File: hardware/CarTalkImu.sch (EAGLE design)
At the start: 11 parts, among them J4 1X10, J5 1X10, U3 MPU9250, U4 NEO-M8

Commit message: Finalized Rev 1A schematic and layout.
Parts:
- added C1, C3, C4, C5, C6, C7: 100n, CarTalkImu:C-USC0603
- added C10, C8: 10u, CarTalkImu:C-USC0603
- added C11, C9: 1u, CarTalkImu:C-USC0603
- added C2: 10n, CarTalkImu:C-USC0603
- added R1, R2, R3, R4, R5: 10k, CarTalkImu:R-US_R0603
- added R10, R11, R6, R7, R8, R9: 220, CarTalkImu:R-US_R0603
- added U1: LPS22HB, CarTalkImu:LPS22HB
- added X1: (no value), CarTalkImu:ESP-12
- U4: value NEO-M8 -> CAM-M8; device CarTalkImu:NEO-M8 -> CarTalkImu:CAM-M8
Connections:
- removed net XB_MULT2: J5.5
- removed net XB_MULT3: J5.9
- removed net XB_MULT5: J4.8
- removed net XB_MULT6: J5.10
- new net N$10: R6.2, U4.RXD/MOSI
- new net N$11: R7.2, U4.TXD/MISO
- new net N$12: R8.2, U4.SCL/SCLK
- new net N$13: R9.2, U4.SDA/CS
- new net N$14: U4.RF_IN, U4.RF_OUT
- new net N$15: R10.2, X1.TXD
- new net N$16: R11.2, X1.RXD
- new net N$4: C1.1, U3.REGOUT
- new net N$6: R1.1, X1.GPIO0
- new net N$7: R2.1, X1.GPIO2
- new net N$8: R3.1, X1.GPIO15
- new net N$9: R4.1, X1.CH_PD
- new net XB_MULT2/PRESS_CS: J5.5, U1.CS
- new net XB_MULT3/TMPLSE: J5.9, U4.TMPLSE
- new net XB_MULT5/MPU_CS: J4.8, U3./CS
- new net XB_MULT6/GPS_CS: J5.10, R9.1
- net +3V3: now also C10.1, C11.1, C2.1, C3.1, C4.1, C5.1, C7.1, C8.1, C9.1, R1.2, R2.2, R4.2, R5.2, U1.VDD, U1.VDD_IO, U3.RESV_1, U3.VDD, U3.VDDIO, U4.VCC, U4.VCC_IO, U4.V_BCKP, X1.VCC
- net DGND: now also C1.2, C10.2, C11.2, C2.2, C3.2, C4.2, C5.2, C6.2, C7.2, C8.2, C9.2, R3.2, U1.GND, U3.FSYNC, U3.GND, U3.RESV_20, U4.D_SEL, U4.GND, X1.GND
- net SPI0_CLK: now also R8.1, U1.SCL/SPC, U3.SCL/SCLK
- net SPI0_MISO: now also R7.1, U1.SDO/SA0, U3.AD0/SDO
- net SPI0_MOSI: now also R6.1, U1.SDA/SDI/SDO, U3.SDA/SDI
- net XB_NRST: now also C6.1, R5.1, U4./RST, X1.RESET
- net XB_UART_RX: now also R10.1
- net XB_UART_TX: now also R11.1
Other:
- moved on the sheet: U3

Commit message: Re-finalized design and layout.
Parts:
- X1: value (none) -> ESP-12
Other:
- moved on the sheet: C10, C11, C5, C6, C7, C8, C9, R1, R10, R11, R2, R3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

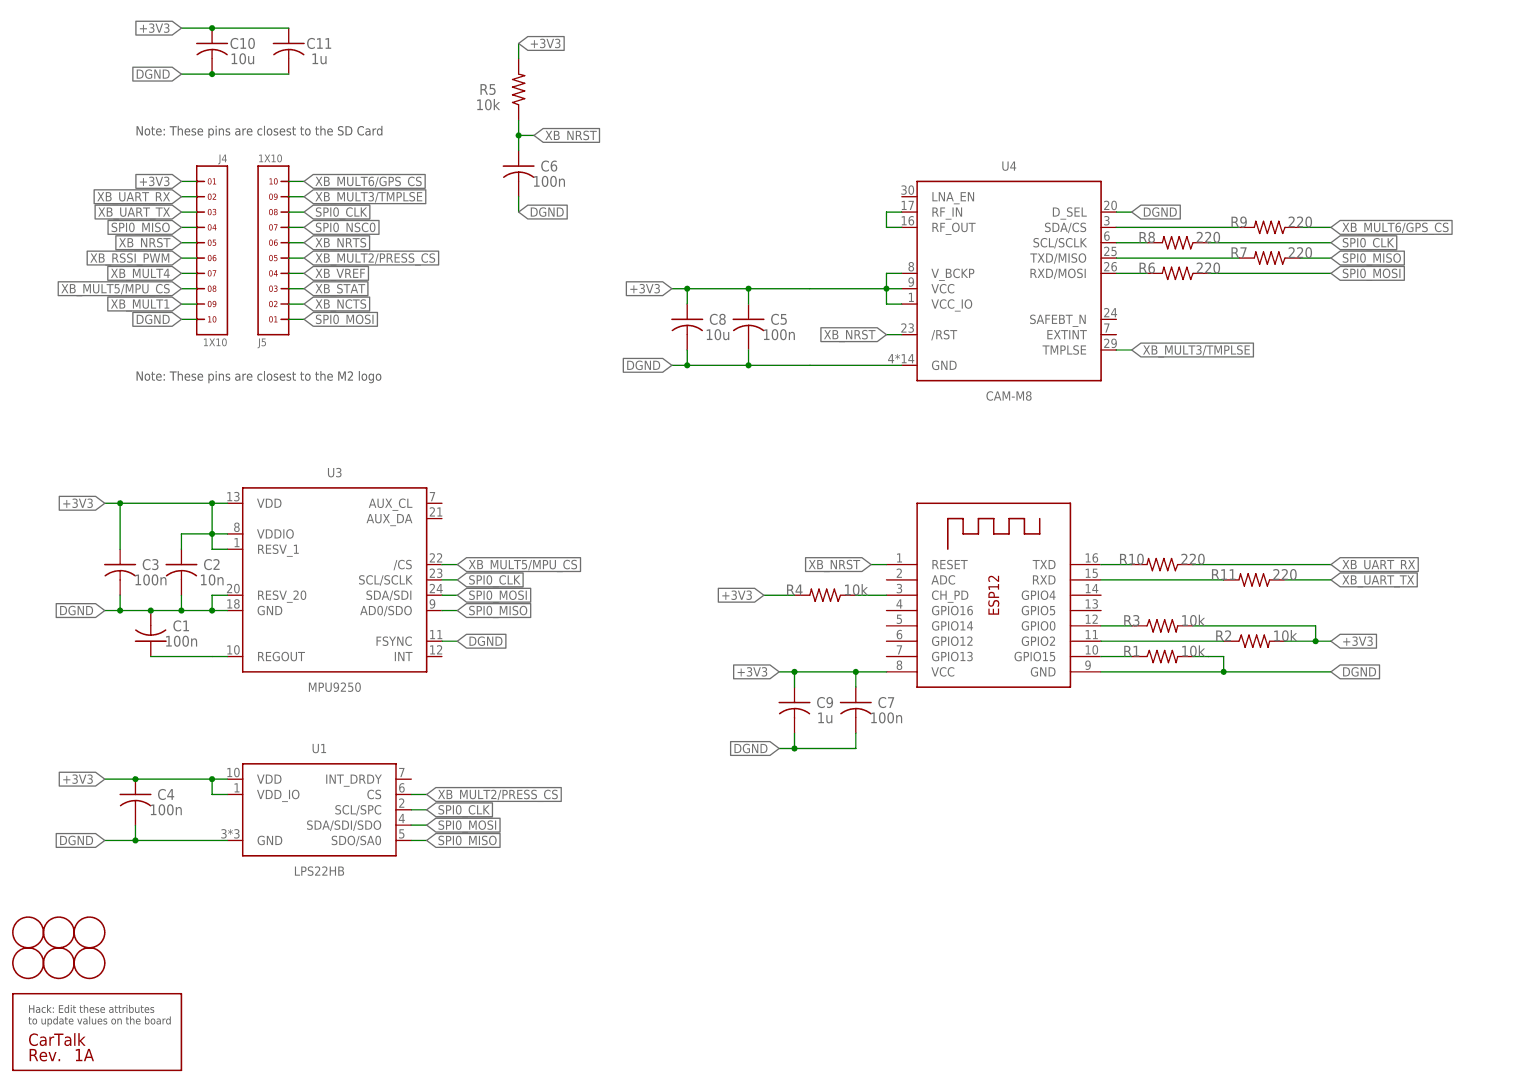
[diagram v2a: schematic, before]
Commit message: Replaced LPS22 part with BME680 part. Upated board layout.
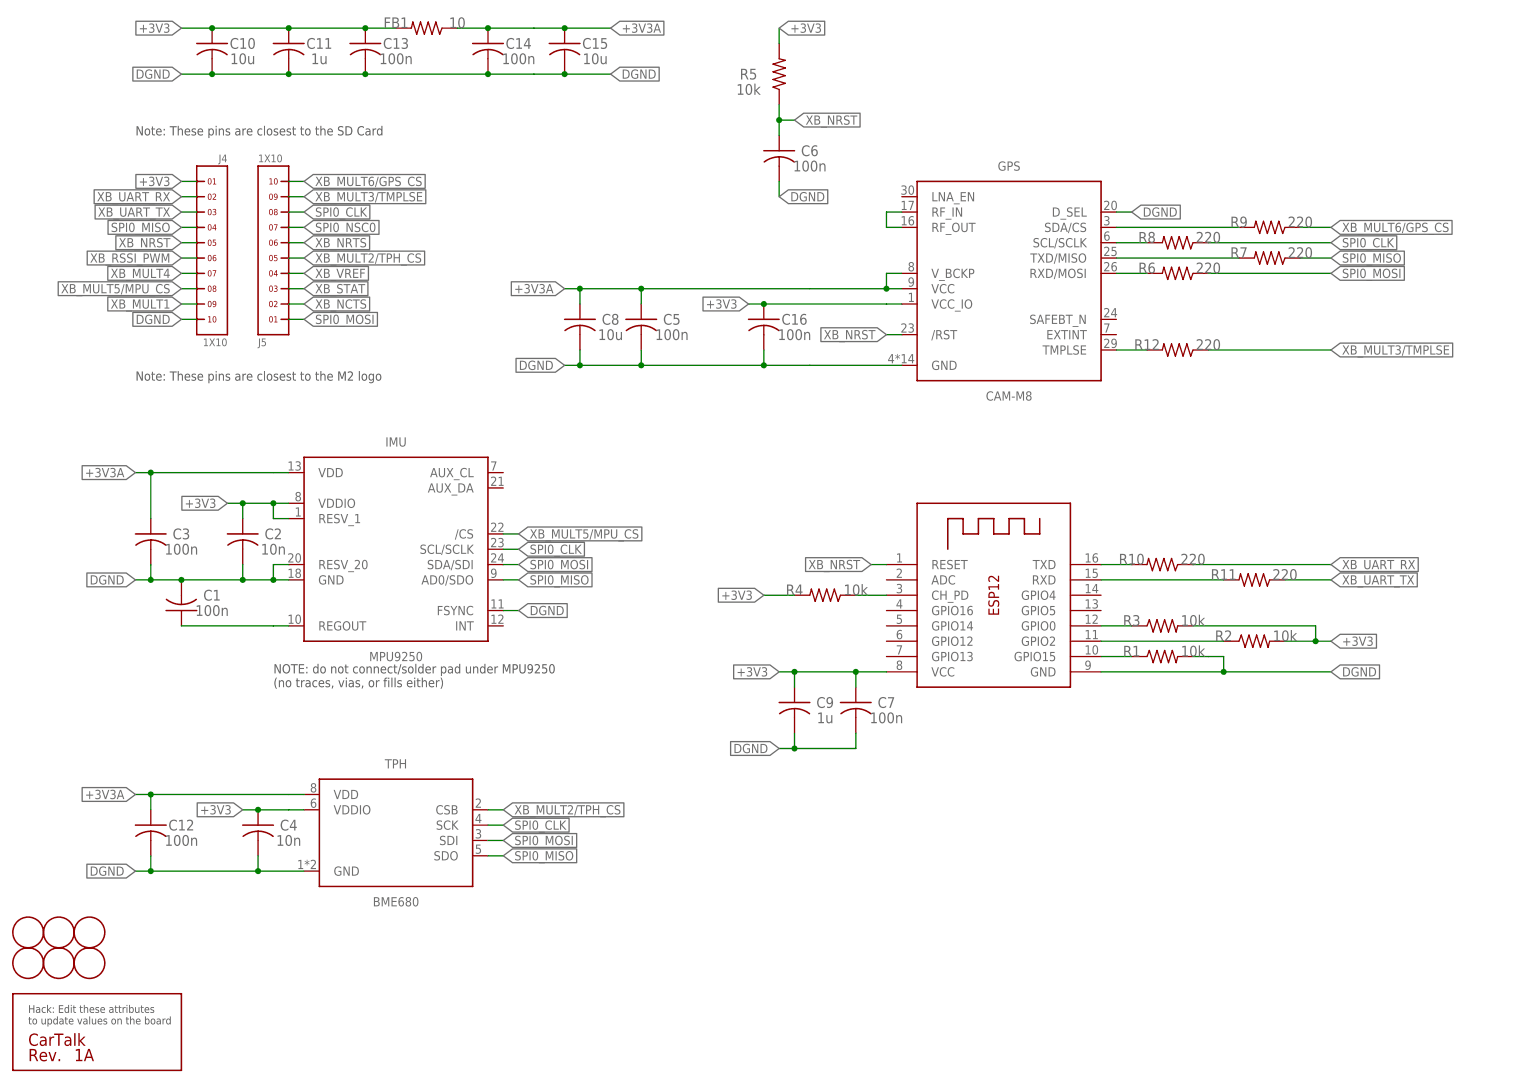
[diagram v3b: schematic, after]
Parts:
- removed U1: LPS22HB, CarTalkImu:LPS22HB
- removed U3: MPU9250, CarTalkImu:MPU9250
- added C12, C13, C14, C16: 100n, CarTalkImu:C-USC0603
- added C15: 10u, CarTalkImu:C-USC0805
- added FB1: 10, CarTalkImu:R-US_R0603
- added IMU: MPU9250, CarTalkImu:MPU9250
- added R12: 220, CarTalkImu:R-US_R0603
- added TPH: BME680, CarTalkImu:BME680
- C10, C8: device CarTalkImu:C-USC0603 -> CarTalkImu:C-USC0805
- C4: value 100n -> 10n
- renumbered U4 to GPS, X1 to WIFI
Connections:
- removed net XB_MULT2/PRESS_CS: J5.5, U1.CS
- new net +3V3A: C12.1, C14.1, C15.1, C3.1, C5.1, C8.1, FB1.1, GPS.VCC, GPS.V_BCKP, IMU.VDD, TPH.VDD
- new net N$18: GPS.TMPLSE, R12.2
- new net XB_MULT2/TPH_CS: J5.5, TPH.CSB
- net +3V3: now also C13.1, C16.1, FB1.2, IMU.RESV_1, IMU.VDDIO, TPH.VDDIO; no longer C3.1, C5.1, C8.1, GPS.VCC, GPS.V_BCKP, U1.VDD, U1.VDD_IO, U3.RESV_1, U3.VDD, U3.VDDIO
- net DGND: now also C12.2, C13.2, C14.2, C15.2, C16.2, IMU.FSYNC, IMU.GND, IMU.RESV_20, TPH.GND; no longer U1.GND, U3.FSYNC, U3.GND, U3.RESV_20
- net N$4: now also IMU.REGOUT; no longer U3.REGOUT
- net SPI0_CLK: now also IMU.SCL/SCLK, TPH.SCK; no longer U1.SCL/SPC, U3.SCL/SCLK
- net SPI0_MISO: now also IMU.AD0/SDO, TPH.SDO; no longer U1.SDO/SA0, U3.AD0/SDO
- net SPI0_MOSI: now also IMU.SDA/SDI, TPH.SDI; no longer U1.SDA/SDI/SDO, U3.SDA/SDI
- net XB_MULT3/TMPLSE: now also R12.1; no longer GPS.TMPLSE
- net XB_MULT5/MPU_CS: now also IMU./CS; no longer U3./CS
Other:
- note added: "NOTE: do not connect/solder pad under MPU9250 (no traces, vias, or fills either)"
- moved on the sheet: C1, C2, C3, C4, C5, C6, C8, R5

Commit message: Fixed minor layout/DFM issues
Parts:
- renumbered IMU to MPU
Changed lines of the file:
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@@
 <grid distance="0.1" unitdist="inch" unit="inch" style="lines" multiple="1" display="no" altdistance="0.01" altunitdist="inch" altunit="inch"/>
 <layers>
-<layer number="1" name="Top" color="4" fill="1" visible="yes" active="no"/>
-<layer number="2" name="Route2" color="1" fill="3" visible="yes" active="no"/>
-<layer number="15" name="Route15" color="4" fill="6" visible="yes" active="no"/>
-<layer number="16" name="Bottom" color="1" fill="1" visible="yes" active="no"/>
-<layer number="17" name="Pads" color="2" fill="1" visible="yes" active="no"/>
-<layer number="18" name="Vias" color="2" fill="1" visible="yes" active="no"/>
-<layer number="19" name="Unrouted" color="6" fill="1" visible="yes" active="no"/>
-<layer number="20" name="Dimension" color="15" fill="1" visible="yes" active="no"/>
-<layer number="21" name="tPlace" color="7" fill="1" visible="yes" active="no"/>
-<layer number="22" name="bPlace" color="7" fill="1" visible="yes" active="no"/>
-<layer number="23" name="tOrigins" color="15" fill="1" visible="yes" active="no"/>
-<layer number="24" name="bOrigins" color="15" fill="1" visible="yes" active="no"/>
-<layer number="25" name="tNames" color="7" fill="1" visible="yes" active="no"/>
-<layer number="26" name="bNames" color="7" fill="1" visible="yes" active="no"/>
-<layer number="27" name="tValues" color="7" fill="1" visible="yes" active="no"/>
-<layer number="28" name="bValues" color="7" fill="1" visible="yes" active="no"/>
+<layer number="1" name="Top" color="4" fill="1" visible="no" active="no"/>
+<layer number="2" name="Route2" color="1" fill="3" visible="no" active="no"/>
+<layer number="15" name="Route15" color="4" fill="6" visible="no" active="no"/>
+<layer number="16" name="Bottom" color="1" fill="1" visible="no" active="no"/>
+<layer number="17" name="Pads" color="2" fill="1" visible="no" active="no"/>
+<layer number="18" name="Vias" color="2" fill="1" visible="no" active="no"/>
+<layer number="19" name="Unrouted" color="6" fill="1" visible="no" active="no"/>
+<layer number="20" name="Dimension" color="15" fill="1" visible="no" active="no"/>
+<layer number="21" name="tPlace" color="7" fill="1" visible="no" active="no"/>
+<layer number="22" name="bPlace" color="7" fill="1" visible="no" active="no"/>
+<layer number="23" name="tOrigins" color="15" fill="1" visible="no" active="no"/>
+<layer number="24" name="bOrigins" color="15" fill="1" visible="no" active="no"/>
+<layer number="25" name="tNames" color="7" fill="1" visible="no" active="no"/>
+<layer number="26" name="bNames" color="7" fill="1" visible="no" active="no"/>
+<layer number="27" name="tValues" color="7" fill="1" visible="no" active="no"/>
+<layer number="28" name="bValues" color="7" fill="1" visible="no" active="no"/>
 <layer number="29" name="tStop" color="7" fill="3" visible="no" active="no"/>
 <layer number="30" name="bStop" color="7" fill="6" visible="no" active="no"/>
@@
 <layer number="35" name="tGlue" color="7" fill="4" visible="no" active="no"/>
 <layer number="36" name="bGlue" color="7" fill="5" visible="no" active="no"/>
-<layer number="37" name="tTest" color="7" fill="1" visible="yes" active="no"/>
-<layer number="38" name="bTest" color="7" fill="1" visible="yes" active="no"/>
+<layer number="37" name="tTest" color="7" fill="1" visible="no" active="no"/>
+<layer number="38" name="bTest" color="7" fill="1" visible="no" active="no"/>
 <layer number="39" name="tKeepout" color="4" fill="11" visible="no" active="no"/>
 <layer number="40" name="bKeepout" color="1" fill="11" visible="no" active="no"/>
@@
 <layer number="44" name="Drills" color="7" fill="1" visible="no" active="no"/>
 <layer number="45" name="Holes" color="7" fill="1" visible="no" active="no"/>
-<layer number="46" name="Milling" color="3" fill="1" visible="yes" active="no"/>
-<layer number="47" name="Measures" color="7" fill="1" visible="yes" active="no"/>
-<layer number="48" name="Document" color="7" fill="1" visible="yes" active="no"/>
-<layer number="49" name="Reference" color="7" fill="1" visible="yes" active="no"/>
-<layer number="50" name="dxf" color="7" fill="1" visible="yes" active="no"/>
-<layer number="51" name="tDocu" color="7" fill="1" visible="yes" active="no"/>
-<layer number="52" name="bDocu" color="7" fill="1" visible="yes" active="no"/>
-<layer number="53" name="tGND_GNDA" color="7" fill="9" visible="yes" active="no"/>
-<layer number="54" name="bGND_GNDA" color="1" fill="9" visible="yes" active="no"/>
-<layer number="56" name="wert" color="7" fill="1" visible="yes" active="no"/>
-<layer number="57" name="tCAD" color="7" fill="1" visible="yes" active="no"/>
+<layer number="46" name="Milling" color="3" fill="1" visible="no" active="no"/>
+<layer number="47" name="Measures" color="7" fill="1" visible="no" active="no"/>
+<layer number="48" name="Document" color="7" fill="1" visible="no" active="no"/>
+<layer number="49" name="Reference" color="7" fill="1" visible="no" active="no"/>
+<layer number="50" name="dxf" color="7" fill="1" visible="no" active="no"/>
+<layer number="51" name="tDocu" color="7" fill="1" visible="no" active="no"/>
+<layer number="52" name="bDocu" color="7" fill="1" visible="no" active="no"/>
+<layer number="53" name="tGND_GNDA" color="7" fill="9" visible="no" active="no"/>
+<layer number="54" name="bGND_GNDA" color="1" fill="9" visible="no" active="no"/>
+<layer number="56" name="wert" color="7" fill="1" visible="no" active="no"/>
+<layer number="57" name="tCAD" color="7" fill="1" visible="no" active="no"/>
 <layer number="90" name="Modules" color="5" fill="1" visible="yes" active="yes"/>
 <layer number="91" name="Nets" color="2" fill="1" visible="yes" active="yes"/>
@@
 <part name="J4" library="CarTalkImu" deviceset="1X10" device=""/>
 <part name="J5" library="CarTalkImu" deviceset="1X10" device=""/>
-<part name="IMU" library="CarTalkImu" deviceset="MPU9250" device=""/>
+<part name="MPU" library="CarTalkImu" deviceset="MPU9250" device=""/>
 <part name="GPS" library="CarTalkImu" deviceset="CAM-M8" device=""/>
 <part name="FRAME1" library="CarTalkImu" deviceset="LETTER_L" device="">
@@
 <instance part="J4" gate="G$1" x="38.1" y="139.7" rot="MR0"/>
 <instance part="J5" gate="G$1" x="48.26" y="142.24" rot="MR180"/>
-<instance part="IMU" gate="G$1" x="68.58" y="91.44"/>
+<instance part="MPU" gate="G$1" x="68.58" y="91.44"/>
 <instance part="GPS" gate="G$1" x="170.18" y="137.16"/>
 <instance part="FRAME1" gate="G$1" x="0" y="0"/>
@@
 </segment>
 <segment>
-<pinref part="IMU" gate="G$1" pin="VDDIO"/>
+<pinref part="MPU" gate="G$1" pin="VDDIO"/>
 <wire x1="50.8" y1="99.06" x2="48.26" y2="99.06" width="0.1524" layer="91"/>
-<pinref part="IMU" gate="G$1" pin="RESV_1"/>
+<pinref part="MPU" gate="G$1" pin="RESV_1"/>
 <wire x1="50.8" y1="96.52" x2="48.26" y2="96.52" width="0.1524" layer="91"/>
 <wire x1="48.26" y1="96.52" x2="48.26" y2="99.06" width="0.1524" layer="91"/>
@@
 <wire x1="88.9" y1="86.36" x2="86.36" y2="86.36" width="0.1524" layer="91"/>
 <label x="88.9" y="86.36" size="1.524" layer="95" xref="yes"/>
-<pinref part="IMU" gate="G$1" pin="AD0/SDO"/>
+<pinref part="MPU" gate="G$1" pin="AD0/SDO"/>
 </segment>
 <segment>
@@
 </segment>
 <segment>
-<pinref part="IMU" gate="G$1" pin="/CS"/>
+<pinref part="MPU" gate="G$1" pin="/CS"/>
 <wire x1="86.36" y1="93.98" x2="88.9" y2="93.98" width="0.1524" layer="91"/>
 <label x="88.9" y="93.98" size="1.524" layer="95" xref="yes"/>
@@
 <wire x1="50.8" y1="86.36" x2="48.26" y2="86.36" width="0.1524" layer="91"/>
 <label x="25.4" y="86.36" size="1.524" layer="95" rot="R180" xref="yes"/>
-<pinref part="IMU" gate="G$1" pin="RESV_20"/>
+<pinref part="MPU" gate="G$1" pin="RESV_20"/>
 <wire x1="48.26" y1="86.36" x2="43.18" y2="86.36" width="0.1524" layer="91"/>
 <wire x1="43.18" y1="86.36" x2="33.02" y2="86.36" width="0.1524" layer="91"/>
@@
 <pinref part="C1" gate="G$1" pin="2"/>
 <junction x="33.02" y="86.36"/>
-<pinref part="IMU" gate="G$1" pin="GND"/>
+<pinref part="MPU" gate="G$1" pin="GND"/>
 </segment>
 <segment>
@@
 </segment>
 <segment>
-<pinref part="IMU" gate="G$1" pin="FSYNC"/>
+<pinref part="MPU" gate="G$1" pin="FSYNC"/>
 <wire x1="86.36" y1="81.28" x2="88.9" y2="81.28" width="0.1524" layer="91"/>
 <label x="88.9" y="81.28" size="1.524" layer="95" xref="yes"/>
@@
 <wire x1="86.36" y1="91.44" x2="88.9" y2="91.44" width="0.1524" layer="91"/>
 <label x="88.9" y="91.44" size="1.524" layer="95" xref="yes"/>
-<pinref part="IMU" gate="G$1" pin="SCL/SCLK"/>
+<pinref part="MPU" gate="G$1" pin="SCL/SCLK"/>
 </segment>
 <segment>
@@
 <wire x1="86.36" y1="88.9" x2="88.9" y2="88.9" width="0.1524" layer="91"/>
 <label x="88.9" y="88.9" size="1.524" layer="95" xref="yes"/>
-<pinref part="IMU" gate="G$1" pin="SDA/SDI"/>
+<pinref part="MPU" gate="G$1" pin="SDA/SDI"/>
 </segment>
 <segment>
@@
 <net name="N$4" class="0">
 <segment>
-<pinref part="IMU" gate="G$1" pin="REGOUT"/>
+<pinref part="MPU" gate="G$1" pin="REGOUT"/>
 <wire x1="50.8" y1="78.74" x2="48.26" y2="78.74" width="0.1524" layer="91"/>
 <pinref part="C1" gate="G$1" pin="1"/>
@@
 <wire x1="27.94" y1="96.52" x2="27.94" y2="104.14" width="0.1524" layer="91"/>
 <junction x="27.94" y="104.14"/>
-<pinref part="IMU" gate="G$1" pin="VDD"/>
-</segment>
-<segment>
+<pinref part="MPU" gate="G$1" pin="VDD"/>
+</segment>
+<segment>
